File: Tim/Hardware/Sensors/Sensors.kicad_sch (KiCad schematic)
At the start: 10 parts, among them U6 ICM-20948, U6 MS5607-02BA

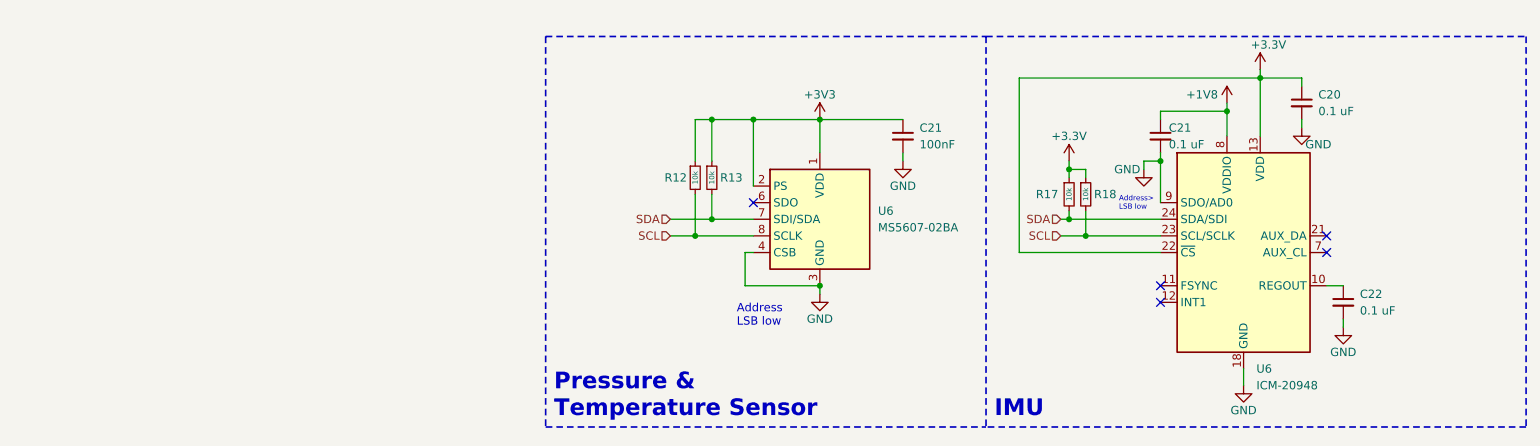
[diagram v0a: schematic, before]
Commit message: Some organization and connectors for external stuffs
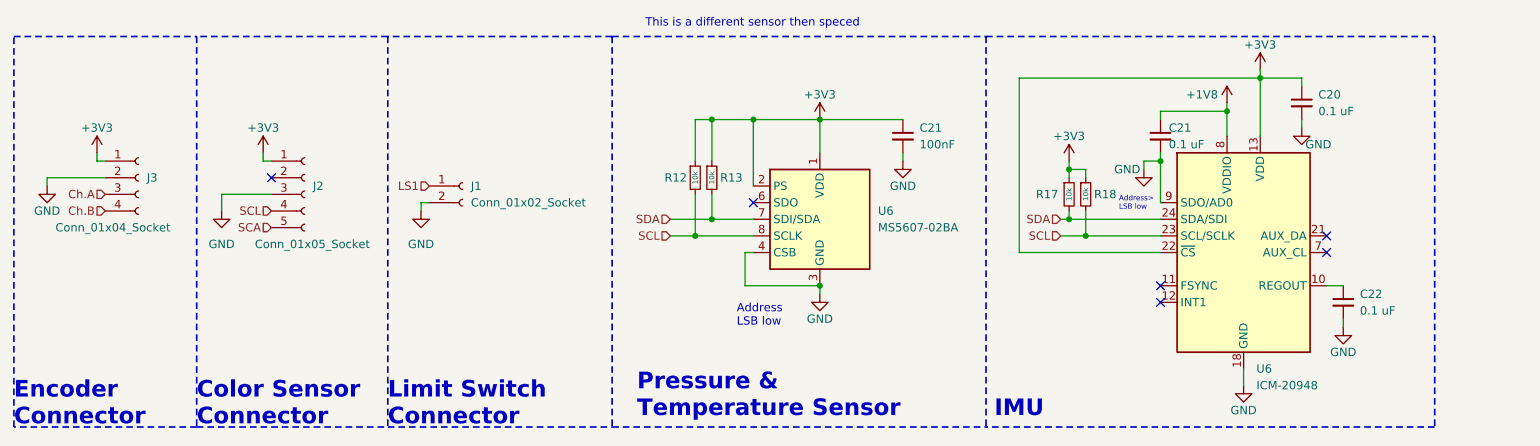
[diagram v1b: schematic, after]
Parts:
- added J1: Conn_01x02_Socket, symbol Connector:Conn_01x02_Socket
- added J2: Conn_01x05_Socket, symbol Connector:Conn_01x05_Socket
- added J3: Conn_01x04_Socket, symbol Connector:Conn_01x04_Socket
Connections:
- net +3.3V is gone; now on net +3V3: C20.1, R17.1, R18.1, U6.13 (VDD), U6.22 (~{CS})
- net +3V3: now also J2.1 (Pin_1), J3.1 (Pin_1)
- net GND: now also J1.2 (Pin_2), J2.3 (Pin_3), J3.2 (Pin_2)
- net SCL: now also J2.4 (Pin_4)
- new net Ch.A: J3.3 (Pin_3)
- new net Ch.B: J3.4 (Pin_4)
- new net LS1: J1.1 (Pin_1)
- new net SCA: J2.5 (Pin_5)
- no-connect marks 5 -> 6
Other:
- note added: "Color Sensor Connector"
- note added: "Encoder Connector"
- note added: "Limit Switch Connector"
- note added: "This is a different sensor then speced"
